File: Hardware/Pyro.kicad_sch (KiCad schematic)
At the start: 0 parts

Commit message: Added pyro circuit
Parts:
- added D3: DST1550S, Package_TO_SOT_SMD:TO-277B, symbol Device:D_Schottky_AAK
- added D4: RED_LED, LED_SMD:LED_0603_1608Metric, symbol Device:LED
- added D5: 954-S-102T, Diode_SMD:D_1206_3216Metric, symbol Device:D
- added Firing1: EMERALD_LED, LED_SMD:LED_0402_1005Metric, symbol Device:LED
- added J3: Conn_01x02_Male, TerminalBlock_Phoenix:TerminalBlock_Phoenix_PT-1,5-2-3.5-H_1x02_P3.50mm_Horizontal, symbol Connector:Conn_01x02_Male
- added Q1: BUK9M11-40EX, Package_TO_SOT_SMD:LFPAK33, symbol Transistor_FET:BUK9M11-40EX
- added R19: 120, Resistor_SMD:R_0402_1005Metric, symbol Device:R
- added R20: 120, Resistor_SMD:R_0603_1608Metric, symbol Device:R
- added U6: 782-TCMT1109, iclr:SOIC127P700X230-4N, symbol Isolator:LTV-247
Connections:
- new net: D4.2 (A), R20.2
- new net: D3.1 (A), D3.2 (A), J3.2 (Pin_2), U6.1
- new net: D5.2 (A), U6.2
- new net: D3.3 (K), Q1.5 (D)
- new net: Firing1.1 (K), R19.1
- new net +3V3: U6.4
- new net Cont1: R20.1, U6.3
- new net GND: D4.1 (K), D5.1 (K), Q1.1 (S), Q1.2 (S), Q1.3 (S), R19.2
- new net Nuke 1: Firing1.2 (A), Q1.4 (G)
- new net V_in: J3.1 (Pin_1)
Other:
- note added: "LTV 247 is a single chip represented by multiple smaller chips"

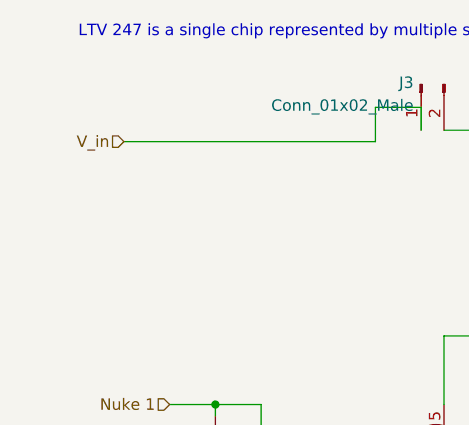
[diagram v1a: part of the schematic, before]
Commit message: Voltage regulation done + used photo ic sensor library
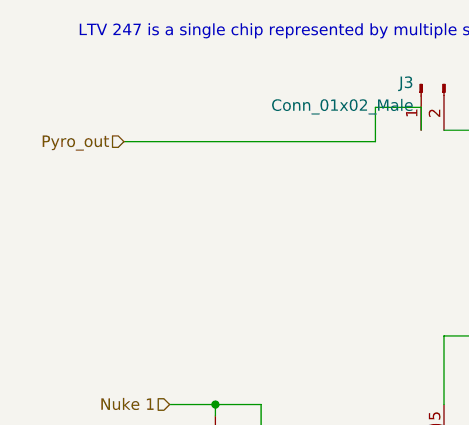
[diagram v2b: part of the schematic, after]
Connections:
- net V_in renamed Pyro_out
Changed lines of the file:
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@@
 		)
 	)
-	(hierarchical_label "V_in"
+	(hierarchical_label "Pyro_out"
 		(shape input)
 		(at 80.01 60.96 180)

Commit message: PCB mid design
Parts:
- removed U6: 782-TCMT1109, iclr:SOIC127P700X230-4N, symbol Isolator:LTV-247
- added U12: TCMT1109, Package_SO:SOP-4_4.4x2.6mm_P1.27mm, symbol Isolator:TCMT1109
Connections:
- net +3V3: now also U12.4
- net Cont1: now also U12.3
- net at D3.1 (A), D3.2 (A), J3.2 (Pin_2): now also U12.1
- net at D5.2 (A): now also U12.2
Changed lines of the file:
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@@
 	(paper "A4")
+	(junction
+		(at 153.67 100.33)
+		(diameter 0)
+		(color 0 0 0 0)
+	)
+	(junction
+		(at 123.19 69.85)
+		(diameter 0)
+		(color 0 0 0 0)
+	)
+	(junction
+		(at 123.19 59.69)
+		(diameter 0)
+		(color 0 0 0 0)
+	)
+	(junction
+		(at 90.17 90.17)
+		(diameter 0)
+		(color 0 0 0 0)
+	)
 	(junction
 		(at 146.05 82.55)
@@
 		(color 0 0 0 0)
 	)
-	(junction
-		(at 153.67 100.33)
-		(diameter 0)
-		(color 0 0 0 0)
-	)
-	(junction
-		(at 123.19 69.85)
-		(diameter 0)
-		(color 0 0 0 0)
-	)
-	(junction
-		(at 123.19 59.69)
-		(diameter 0)
-		(color 0 0 0 0)
-	)
-	(junction
-		(at 90.17 90.17)
-		(diameter 0)
-		(color 0 0 0 0)
-	)
 	(wire
 		(pts
@@
 	(wire
 		(pts
-			(xy 80.01 60.96) (xy 107.95 60.96)
-		)
-		(stroke
-			(width 0)
-			(type default)
-		)
-	)
-	(wire
-		(pts
-			(xy 107.95 57.15) (xy 113.03 57.15)
-		)
-		(stroke
-			(width 0)
-			(type default)
-		)
-	)
-	(wire
-		(pts
-			(xy 113.03 57.15) (xy 113.03 59.69)
-		)
-		(stroke
-			(width 0)
-			(type default)
-		)
-	)
-	(wire
-		(pts
 			(xy 115.57 100.33) (xy 115.57 105.41)
 		)
@@
 	(wire
 		(pts
+			(xy 80.01 59.69) (xy 113.03 59.69)
+		)
+		(stroke
+			(width 0)
+			(type default)
+		)
+	)
+	(wire
+		(pts
 			(xy 123.19 78.74) (xy 123.19 82.55)
 		)
@@
 		(pts
 			(xy 90.17 90.17) (xy 90.17 91.44)
-		)
-		(stroke
-			(width 0)
-			(type default)
-		)
-	)
-	(wire
-		(pts
-			(xy 107.95 60.96) (xy 107.95 57.15)
 		)
 		(stroke
@@
 	(hierarchical_label "Pyro_out"
 		(shape input)
-		(at 80.01 60.96 180)
+		(at 80.01 59.69 180)
 		(fields_autoplaced yes)
 		(effects
@@
 		)
 		(property "Value" "Conn_01x02_Male"
-			(at 112.1918 56.9472 90)
+			(at 120.904 51.562 90)
 			(effects
 				(font
@@
 	)
 	(symbol
+		(lib_id "Isolator:TCMT1109")
+		(at 153.67 80.01 0)
+		(mirror y)
+		(unit 1)
+		(exclude_from_sim no)
+		(in_bom yes)
+		(on_board yes)
+		(dnp no)
+		(property "Reference" "U12"
+			(at 153.67 71.12 0)
+			(effects
+				(font
+					(size 1.27 1.27)
+				)
+			)
+		)
+		(property "Value" "TCMT1109"
+			(at 153.67 73.66 0)
+			(effects
+				(font
+					(size 1.27 1.27)
+				)
+			)
+		)
+		(property "Footprint" "Package_SO:SOP-4_4.4x2.6mm_P1.27mm"
+			(at 153.67 87.63 0)
+			(effects
+				(font
+					(size 1.27 1.27)
+				)
+				(hide yes)
+			)
+		)
+		(property "Datasheet" "http://www.vishay.com/docs/83510/tcmt1100.pdf"
+			(at 153.67 81.28 0)
+			(effects
+				(font
+					(size 1.27 1.27)
+				)
+				(justify left)
+				(hide yes)
+			)
+		)
+		(property "Description" "Optocoupler, Vce 70V, CTR 200-400%, Viso 3750V (RMS), SOP-4"
+			(at 153.67 80.01 0)
+			(effects
+				(font
+					(size 1.27 1.27)
+				)
+				(hide yes)
+			)
+		)
+		(pin "3"
+		)
+		(pin "2"
+		)
+		(pin "1"
+		)
+		(pin "4"
+		)
+		(instances
+			(project ""
+				(path "/7db990e4-92e1-4f99-b4d2-435bbec1ba83/2f4d1188-68cf-4851-a56c-97d43238a03a"
+					(reference "U12")
+					(unit 1)
+				)
+			)
+		)
+	)
+	(symbol
 		(lib_id "Device:R")
 		(at 146.05 86.36 0)
@@
 					(unit 1)
 				)
-			)
-		)
-	)
-	(symbol
-		(lib_id "Isolator:LTV-247")
-		(at 153.67 80.01 0)
-		(mirror y)
-		(unit 1)
-		(exclude_from_sim no)
-		(in_bom yes)
-		(on_board yes)
-		(dnp no)
-		(fields_autoplaced yes)
-		(property "Reference" "U6"
-			(at 153.67 71.374 0)
-			(effects
-				(font
-					(size 1.27 1.27)
-				)
-			)
-		)
-		(property "Value" "782-TCMT1109"
-			(at 153.67 73.914 0)
-			(effects
-				(font
-					(size 1.27 1.27)
-				)
-			)
-		)
-		(property "Footprint" "iclr:SOIC127P700X230-4N"
-			(at 158.75 85.09 0)
-			(effects
-				(font
-					(size 1.27 1.27)
-					(italic yes)
-				)
-				(justify left)
-				(hide yes)
-			)
-		)
-		(property "Datasheet" "https://www.vishay.com/docs/83510/tcmt11.pdf"
-			(at 153.67 80.01 0)
-			(effects
-				(font
-					(size 1.27 1.27)
-				)
-				(justify left)
-				(hide yes)
-			)
-		)
-		(property "Description" ""
-			(at 153.67 80.01 0)
-			(effects
-				(font
-					(size 1.27 1.27)
-				)
-				(hide yes)
-			)
-		)
-		(pin "1"
-		)
-		(pin "3"
-		)
-		(pin "4"
-		)
-		(pin "2"
-		)
-		(pin "13"
-		)
-		(pin "14"
-		)
-		(pin "3"
-		)
-		(pin "4"
-		)
-		(pin "11"
-		)
-		(pin "12"
-		)
-		(pin "5"
-		)
-		(pin "6"
-		)
-		(pin "10"
-		)
-		(pin "7"
-		)
-		(pin "8"
-		)
-		(pin "9"
-		)
-		(instances
-			(project "Main board"
-				(path "/7db990e4-92e1-4f99-b4d2-435bbec1ba83/2f4d1188-68cf-4851-a56c-97d43238a03a"
-					(reference "U6")
-					(unit 1)
-				)

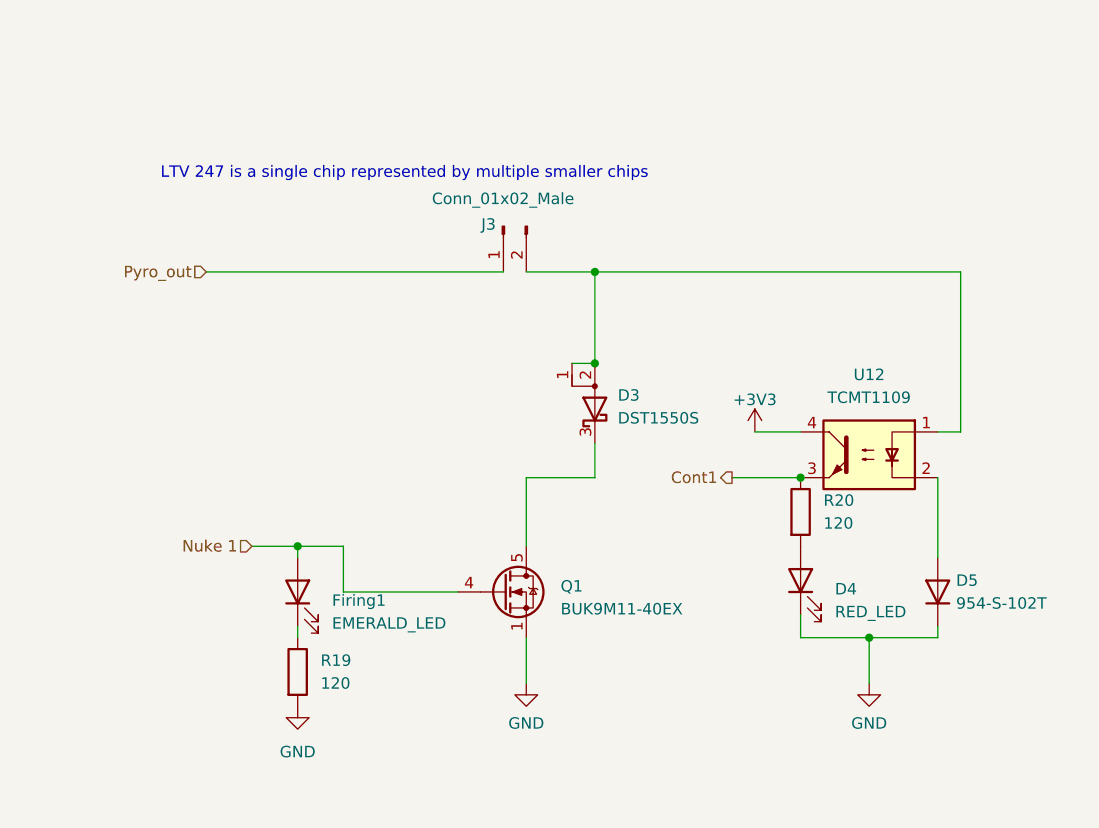
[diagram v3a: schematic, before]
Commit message: Crosshair V1.0
New pyro connectors, silkscreen sorted, mostly connected properly + cool new name and image
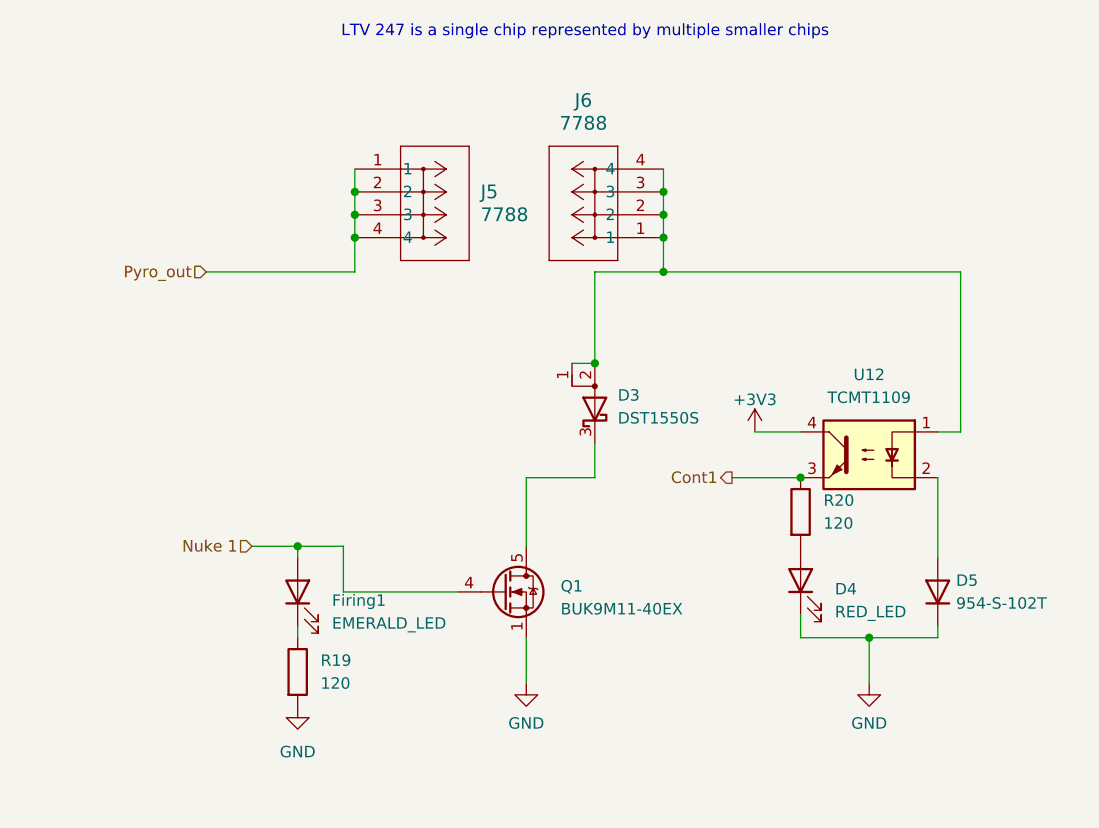
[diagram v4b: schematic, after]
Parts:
- removed J3: Conn_01x02_Male, TerminalBlock_Phoenix:TerminalBlock_Phoenix_PT-1,5-2-3.5-H_1x02_P3.50mm_Horizontal, symbol Connector:Conn_01x02_Male
- added J5, J6: 7788, iclr:CONN_7788_KEY, symbol iclr:7788
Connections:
- net Pyro_out: now also J5.1, J5.2, J5.3, J5.4
- net at D3.1 (A), D3.2 (A), U12.1: now also J6.1, J6.2, J6.3, J6.4
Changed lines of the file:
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@@
 (kicad_sch
-	(version 20231120)
+	(version 20250114)
 	(generator "eeschema")
-	(generator_version "8.0")
+	(generator_version "9.0")
 	(paper "A4")
+	(text "LTV 247 is a single chip represented by multiple smaller chips"
+		(exclude_from_sim no)
+		(at 94.996 33.782 0)
+		(effects
+			(font
+				(size 1.27 1.27)
+			)
+			(justify left bottom)
+		)
+	)
+	(junction
+		(at 130.81 59.69)
+		(diameter 0)
+		(color 0 0 0 0)
+	)
+	(junction
+		(at 96.52 50.8)
+		(diameter 0)
+		(color 0 0 0 0)
+	)
+	(junction
+		(at 130.81 55.88)
+		(diameter 0)
+		(color 0 0 0 0)
+	)
+	(junction
+		(at 130.81 50.8)
+		(diameter 0)
+		(color 0 0 0 0)
+	)
 	(junction
 		(at 153.67 100.33)
@@
 	)
 	(junction
+		(at 96.52 53.34)
+		(diameter 0)
+		(color 0 0 0 0)
+	)
+	(junction
 		(at 123.19 69.85)
 		(diameter 0)
@@
 	)
 	(junction
-		(at 123.19 59.69)
+		(at 130.81 53.34)
 		(diameter 0)
 		(color 0 0 0 0)
@@
 		(color 0 0 0 0)
 	)
-	(wire
-		(pts
-			(xy 123.19 59.69) (xy 163.83 59.69)
+	(junction
+		(at 96.52 55.88)
+		(diameter 0)
+		(color 0 0 0 0)
+	)
+	(wire
+		(pts
+			(xy 123.19 59.69) (xy 130.81 59.69)
+		)
+		(stroke
+			(width 0)
+			(type default)
+		)
+	)
+	(wire
+		(pts
+			(xy 96.52 53.34) (xy 96.52 55.88)
 		)
 		(stroke
@@
 	(wire
 		(pts
+			(xy 130.81 50.8) (xy 130.81 53.34)
+		)
+		(stroke
+			(width 0)
+			(type default)
+		)
+	)
+	(wire
+		(pts
 			(xy 85.09 90.17) (xy 90.17 90.17)
 		)
@@
 	(wire
 		(pts
+			(xy 96.52 48.26) (xy 96.52 50.8)
+		)
+		(stroke
+			(width 0)
+			(type default)
+		)
+	)
+	(wire
+		(pts
 			(xy 90.17 90.17) (xy 95.25 90.17)
 		)
@@
 	(wire
 		(pts
-			(xy 115.57 59.69) (xy 123.19 59.69)
+			(xy 96.52 55.88) (xy 96.52 59.69)
+		)
+		(stroke
+			(width 0)
+			(type default)
+		)
+	)
+	(wire
+		(pts
+			(xy 130.81 55.88) (xy 130.81 59.69)
 		)
 		(stroke
@@
 	(wire
 		(pts
-			(xy 80.01 59.69) (xy 113.03 59.69)
+			(xy 80.01 59.69) (xy 96.52 59.69)
+		)
+		(stroke
+			(width 0)
+			(type default)
+		)
+	)
+	(wire
+		(pts
+			(xy 96.52 50.8) (xy 96.52 53.34)
 		)
 		(stroke
@@
 	(wire
 		(pts
+			(xy 130.81 59.69) (xy 163.83 59.69)
+		)
+		(stroke
+			(width 0)
+			(type default)
+		)
+	)
+	(wire
+		(pts
+			(xy 130.81 48.26) (xy 130.81 50.8)
+		)
+		(stroke
+			(width 0)
+			(type default)
+		)
+	)
+	(wire
+		(pts
 			(xy 146.05 97.79) (xy 146.05 100.33)
 		)
@@
 		)
 	)
-	(text "LTV 247 is a single chip represented by multiple smaller chips"
-		(exclude_from_sim no)
-		(at 74.93 49.53 0)
+	(wire
+		(pts
+			(xy 130.81 53.34) (xy 130.81 55.88)
+		)
+		(stroke
+			(width 0)
+			(type default)
+		)
+	)
+	(hierarchical_label "Nuke 1"
+		(shape input)
+		(at 85.09 90.17 180)
 		(effects
 			(font
 				(size 1.27 1.27)
 			)
-			(justify left bottom)
-		)
-	)
-	(hierarchical_label "Nuke 1"
-		(shape input)
-		(at 85.09 90.17 180)
-		(fields_autoplaced yes)
+			(justify right)
+		)
+	)
+	(hierarchical_label "Cont1"
+		(shape output)
+		(at 138.43 82.55 180)
 		(effects
 			(font
@@
 		)
 	)
-	(hierarchical_label "Cont1"
-		(shape output)
-		(at 138.43 82.55 180)
-		(fields_autoplaced yes)
-		(effects
-			(font
-				(size 1.27 1.27)
-			)
-			(justify right)
-		)
-	)
 	(hierarchical_label "Pyro_out"
 		(shape input)
 		(at 80.01 59.69 180)
-		(fields_autoplaced yes)
 		(effects
 			(font
@@
 	)
 	(symbol
-		(lib_id "Connector:Conn_01x02_Male")
-		(at 113.03 54.61 90)
-		(mirror x)
-		(unit 1)
-		(exclude_from_sim no)
-		(in_bom yes)
-		(on_board yes)
-		(dnp no)
-		(property "Reference" "J3"
-			(at 112.1918 54.4103 90)
-			(effects
-				(font
-					(size 1.27 1.27)
-				)
-				(justify left)
-			)
-		)
-		(property "Value" "Conn_01x02_Male"
-			(at 120.904 51.562 90)
-			(effects
-				(font
-					(size 1.27 1.27)
-				)
-				(justify left)
-			)
-		)
-		(property "Footprint" "TerminalBlock_Phoenix:TerminalBlock_Phoenix_PT-1,5-2-3.5-H_1x02_P3.50mm_Horizontal"
-			(at 113.03 54.61 0)
-			(effects
-				(font
-					(size 1.27 1.27)
-				)
-				(hide yes)
-			)
-		)
-		(property "Datasheet" "~"
-			(at 113.03 54.61 0)
-			(effects
-				(font
-					(size 1.27 1.27)
-				)
-				(hide yes)
-			)
-		)
-		(property "Description" ""
-			(at 113.03 54.61 0)
-			(effects
-				(font
-					(size 1.27 1.27)
-				)
-				(hide yes)
-			)
-		)
-		(pin "1"
-		)
-		(pin "2"
-		)
-		(instances
-			(project "Main board"
-				(path "/7db990e4-92e1-4f99-b4d2-435bbec1ba83/2f4d1188-68cf-4851-a56c-97d43238a03a"
-					(reference "J3")
-					(unit 1)
-				)
-			)
-		)
-	)
-	(symbol
 		(lib_id "Device:D")
 		(at 161.29 95.25 90)
@@
 	)
 	(symbol
+		(lib_id "iclr:7788")
+		(at 96.52 48.26 0)
+		(unit 1)
+		(exclude_from_sim no)
+		(in_bom yes)
+		(on_board yes)
+		(dnp no)
+		(fields_autoplaced yes)
+		(property "Reference" "J5"
+			(at 110.49 50.7999 0)
+			(effects
+				(font
+					(size 1.524 1.524)
+				)
+				(justify left)
+			)
+		)
+		(property "Value" "7788"
+			(at 110.49 53.3399 0)
+			(effects
+				(font
+					(size 1.524 1.524)
+				)
+				(justify left)
+			)
+		)
+		(property "Footprint" "iclr:CONN_7788_KEY"
+			(at 96.52 48.26 0)
+			(effects
+				(font
+					(size 1.27 1.27)
+					(italic yes)
+				)
+				(hide yes)
+			)
+		)
+		(property "Datasheet" "7788"
+			(at 96.52 48.26 0)
+			(effects
+				(font
+					(size 1.27 1.27)
+					(italic yes)
+				)
+				(hide yes)
+			)
+		)
+		(property "Description" ""
+			(at 96.52 48.26 0)
+			(effects
+				(font
+					(size 1.27 1.27)
+				)
+				(hide yes)
+			)
+		)
+		(pin "2"
+		)
+		(pin "1"
+		)
+		(pin "4"
+		)
+		(pin "3"
+		)
+		(instances
+			(project ""
+				(path "/7db990e4-92e1-4f99-b4d2-435bbec1ba83/2f4d1188-68cf-4851-a56c-97d43238a03a"
+					(reference "J5")
+					(unit 1)
+				)
+			)
+		)
+	)
+	(symbol
 		(lib_id "Device:LED")
 		(at 90.17 95.25 90)
@@
 					(unit 1)
 				)
+			)
+		)
+	)
+	(symbol
+		(lib_id "iclr:7788")
+		(at 130.81 55.88 180)
+		(unit 1)
+		(exclude_from_sim no)
+		(in_bom yes)
+		(on_board yes)
+		(dnp no)
+		(fields_autoplaced yes)
+		(property "Reference" "J6"
+			(at 121.92 40.64 0)
+			(effects
+				(font
+					(size 1.524 1.524)
+				)
+			)
+		)
+		(property "Value" "7788"
+			(at 121.92 43.18 0)
+			(effects
+				(font
+					(size 1.524 1.524)
+				)
+			)
+		)
+		(property "Footprint" "iclr:CONN_7788_KEY"
+			(at 130.81 55.88 0)
+			(effects
+				(font
+					(size 1.27 1.27)
+					(italic yes)
+				)
+				(hide yes)
+			)
+		)
+		(property "Datasheet" "7788"
+			(at 130.81 55.88 0)
+			(effects
+				(font
+					(size 1.27 1.27)
+					(italic yes)
+				)
+				(hide yes)
+			)
+		)
+		(property "Description" ""
+			(at 130.81 55.88 0)
+			(effects
+				(font
+					(size 1.27 1.27)
+				)
+				(hide yes)
+			)
+		)
+		(pin "4"
+		)
+		(pin "1"
+		)
+		(pin "2"
+		)
+		(pin "3"
+		)
+		(instances
+			(project ""
+				(path "/7db990e4-92e1-4f99-b4d2-435bbec1ba83/2f4d1188-68cf-4851-a56c-97d43238a03a"
+					(reference "J6")
+					(unit 1)
+				)
